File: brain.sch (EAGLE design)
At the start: 14 parts

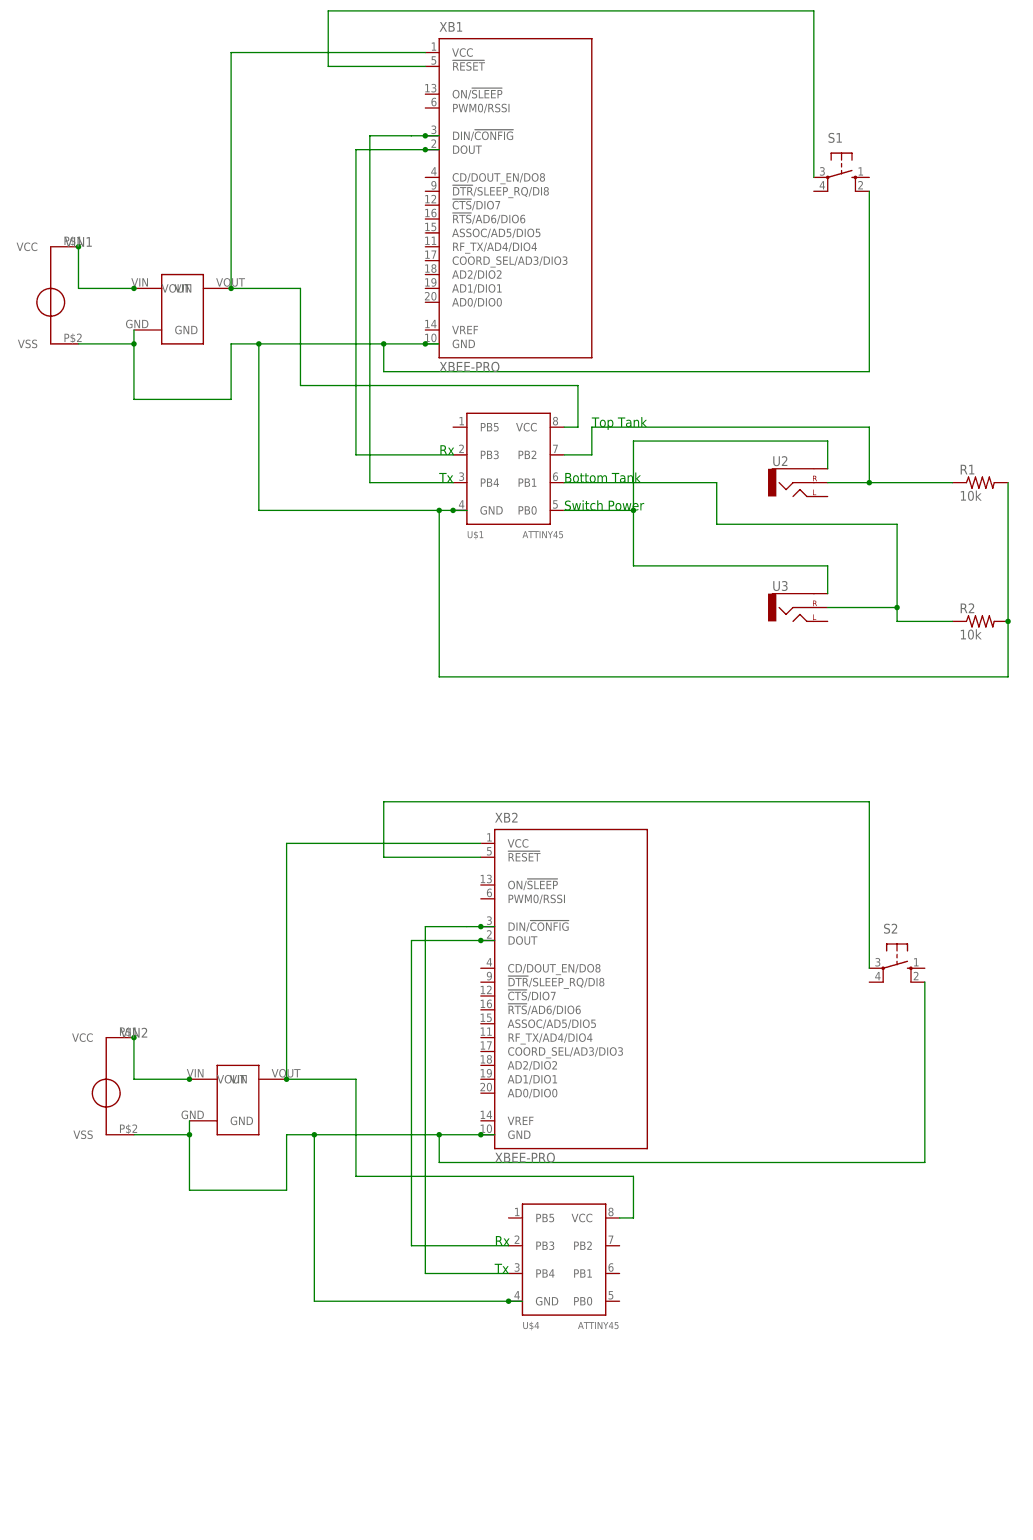
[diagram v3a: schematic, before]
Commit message: Switched the ATTINY45 to the proper package. Added error LED to receiving board. Bypass capacitors added to board. To consider: using vcc/gnd planes for capacitance as well.
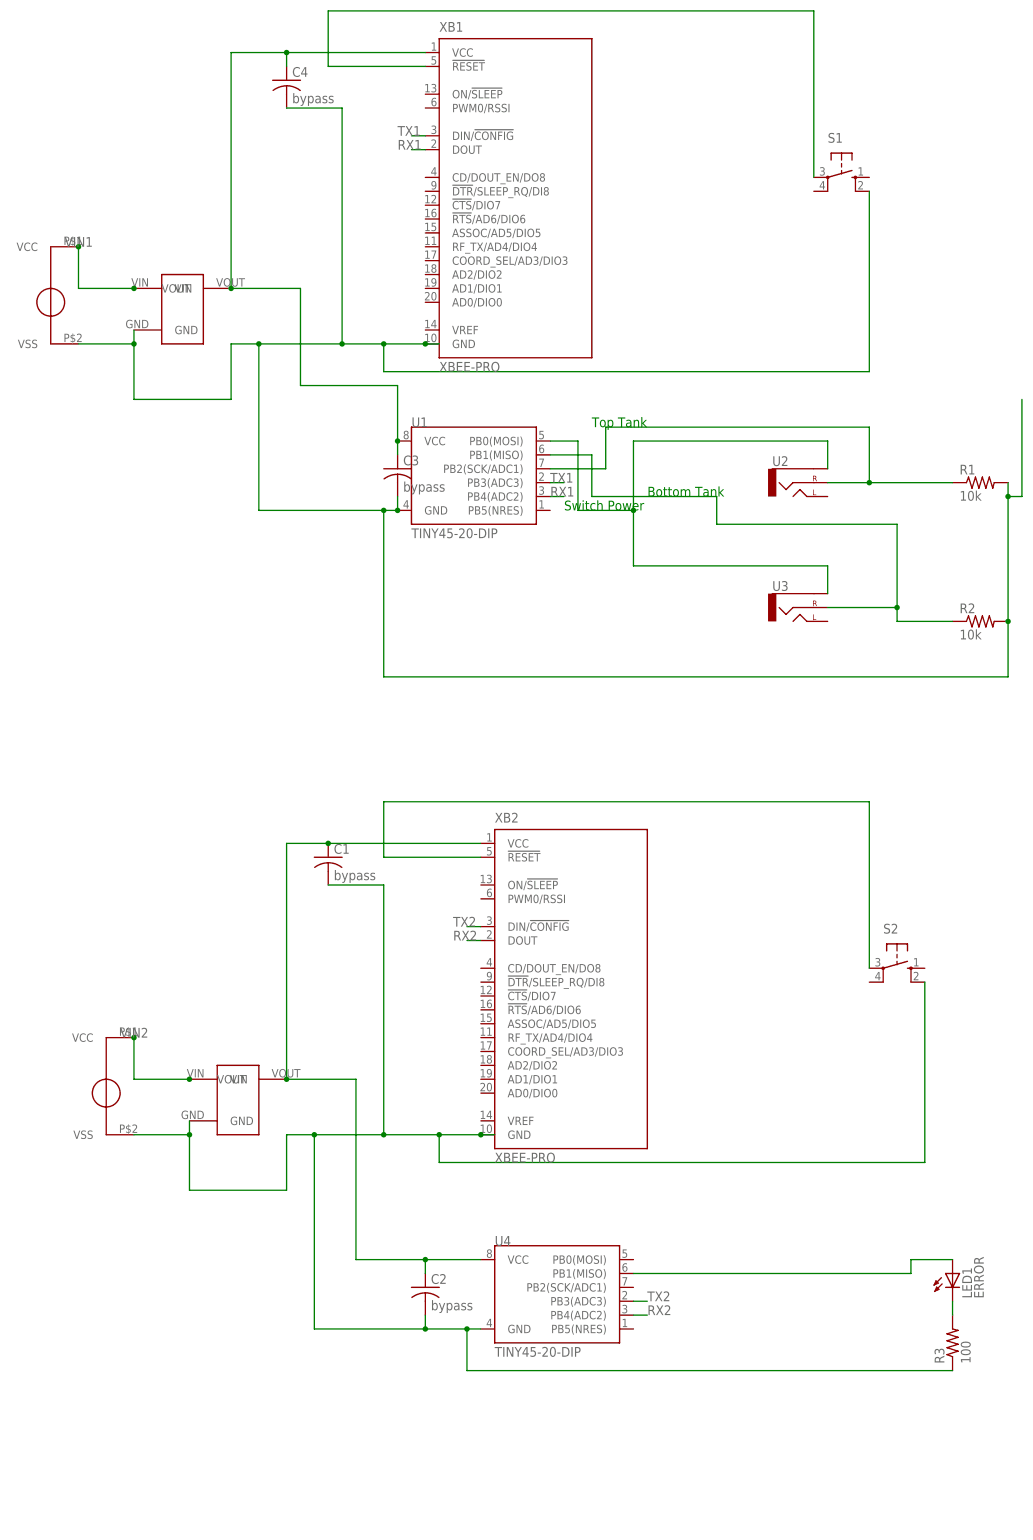
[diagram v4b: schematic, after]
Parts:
- removed U$1, U$4: ATTINY45, attiny45:ATTINY45
- added C1, C2, C3, C4: bypass, rcl:C-US050-025X075
- added LED1: ERROR, led:LED3MM
- added R3: 100, resistor:R-US_0207/10
- added U1, U4: TINY45-20-DIP, SparkFun-DigitalIC:ATTINY45TINY45-20-DIP
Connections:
- removed net N$11: U$1.PB4, XB1.DIN/!CONFIG
- removed net N$14: U$1.PB3, XB1.DOUT
- removed net N$7: U$4.PB4, XB2.DIN/!CONFIG
- removed net N$9: U$4.PB3, XB2.DOUT
- new net N$1: LED1.A, U4.PB1(MISO)
- new net N$5: LED1.C, R3.2
- new net RX1: U1.PB4(ADC2), XB1.DOUT
- new net RX2: U4.PB4(ADC2), XB2.DOUT
- new net TX1: U1.PB3(ADC3), XB1.DIN/!CONFIG
- new net TX2: U4.PB3(ADC3), XB2.DIN/!CONFIG
- net GND1: now also C3.2, C4.2, U1.GND; no longer U$1.GND
- net GND2: now also C1.2, C2.2, R3.1, U4.GND; no longer U$4.GND
- net N$2: now also U1.PB2(SCK/ADC1); no longer U$1.PB2
- net N$3: now also U1.PB1(MISO); no longer U$1.PB1
- net N$4: now also U1.PB0(MOSI); no longer U$1.PB0
- net VCC1: now also C3.1, C4.1, U1.VCC; no longer U$1.VCC
- net VOUT2: now also C1.1, C2.1, U4.VCC; no longer U$4.VCC
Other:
- note removed: "Rx"
- note removed: "Tx"

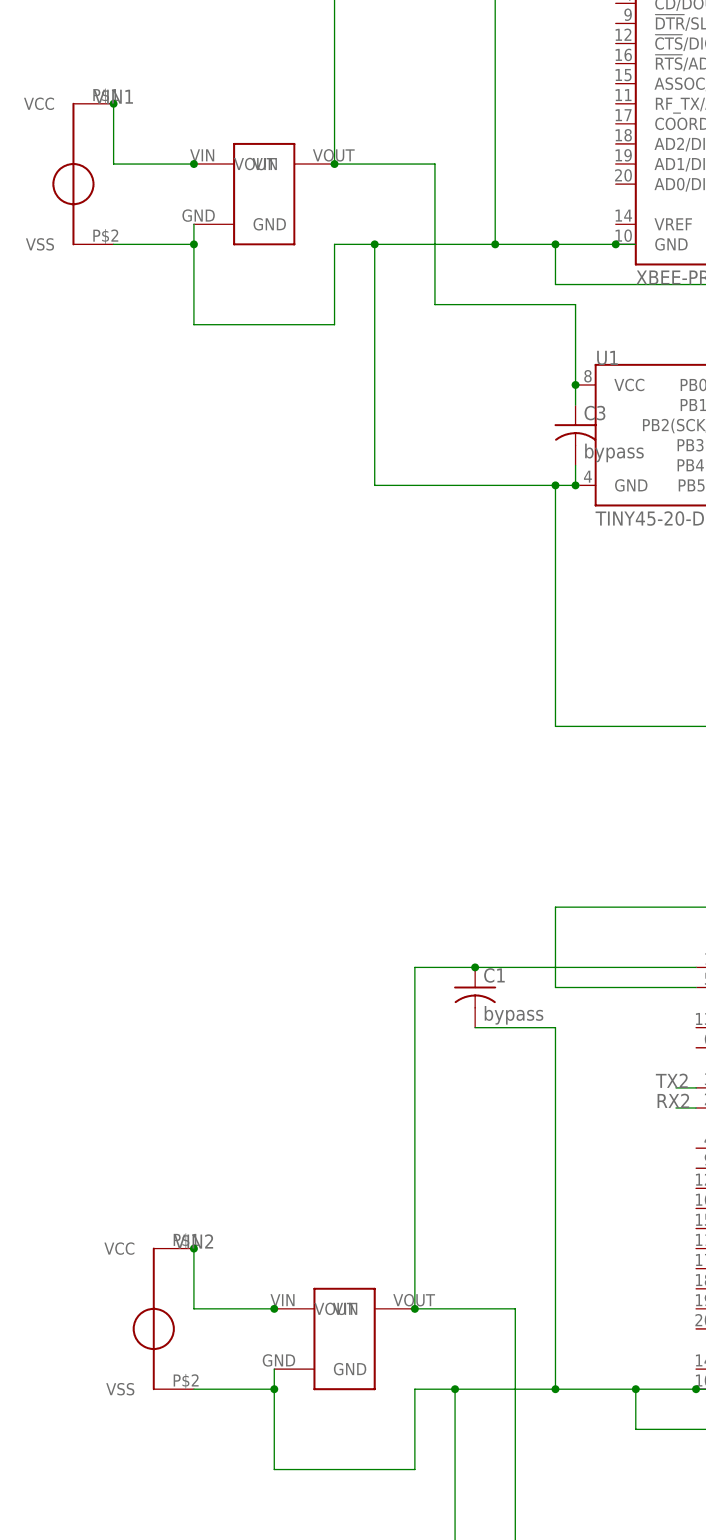
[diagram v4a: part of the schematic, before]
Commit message: Switched the LDO to the ST device.
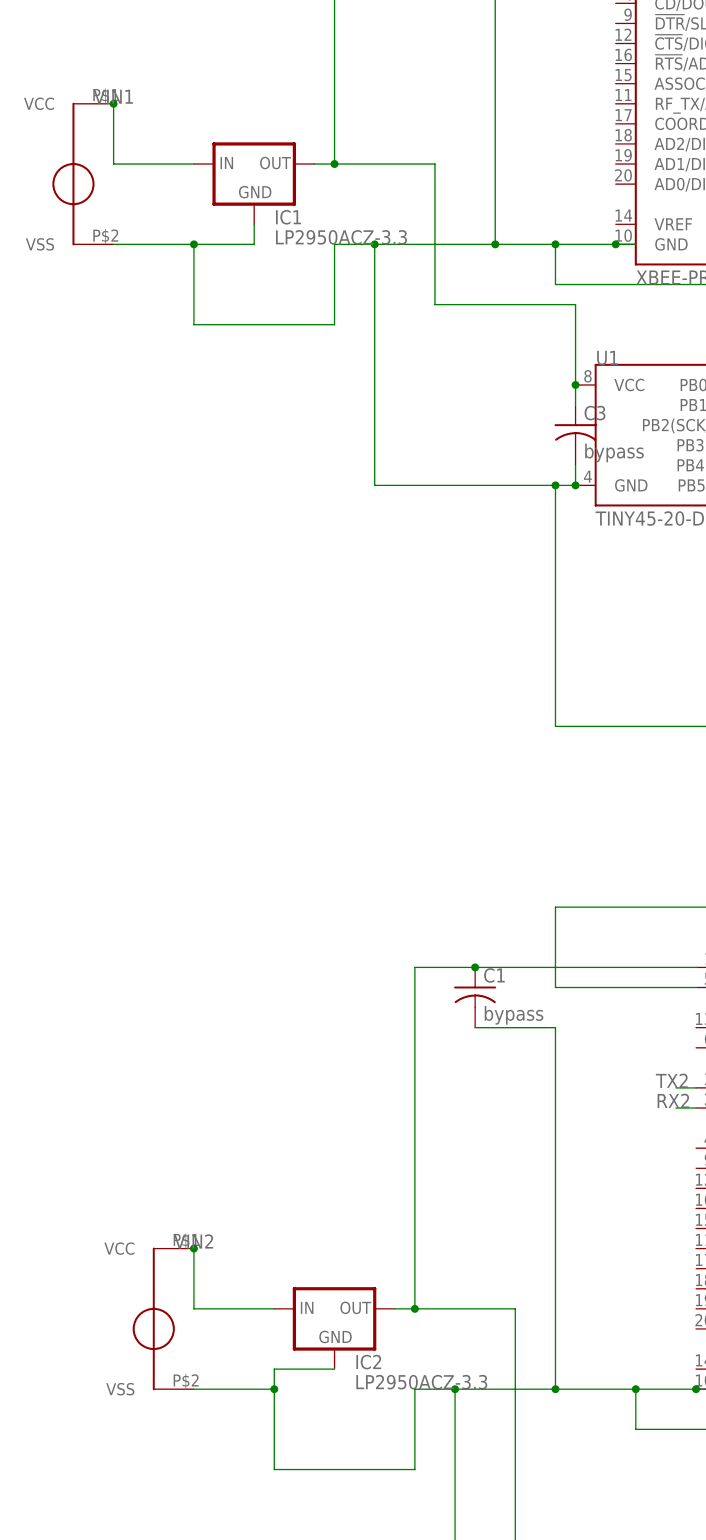
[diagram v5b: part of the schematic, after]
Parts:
- removed U$2, U$5: LP2950, seniordesign:LP2950
- added IC1, IC2: LP2950ACZ-3.3, v-reg:LP2950ACZ-3.3
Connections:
- net GND1: now also IC1.GND; no longer U$2.GND
- net GND2: now also IC2.GND; no longer U$5.GND
- net VCC1: now also IC1.OUT; no longer U$2.VOUT
- net VIN1: now also IC1.IN; no longer U$2.VIN
- net VIN2: now also IC2.IN; no longer U$5.VIN
- net VOUT2: now also IC2.OUT; no longer U$5.VOUT

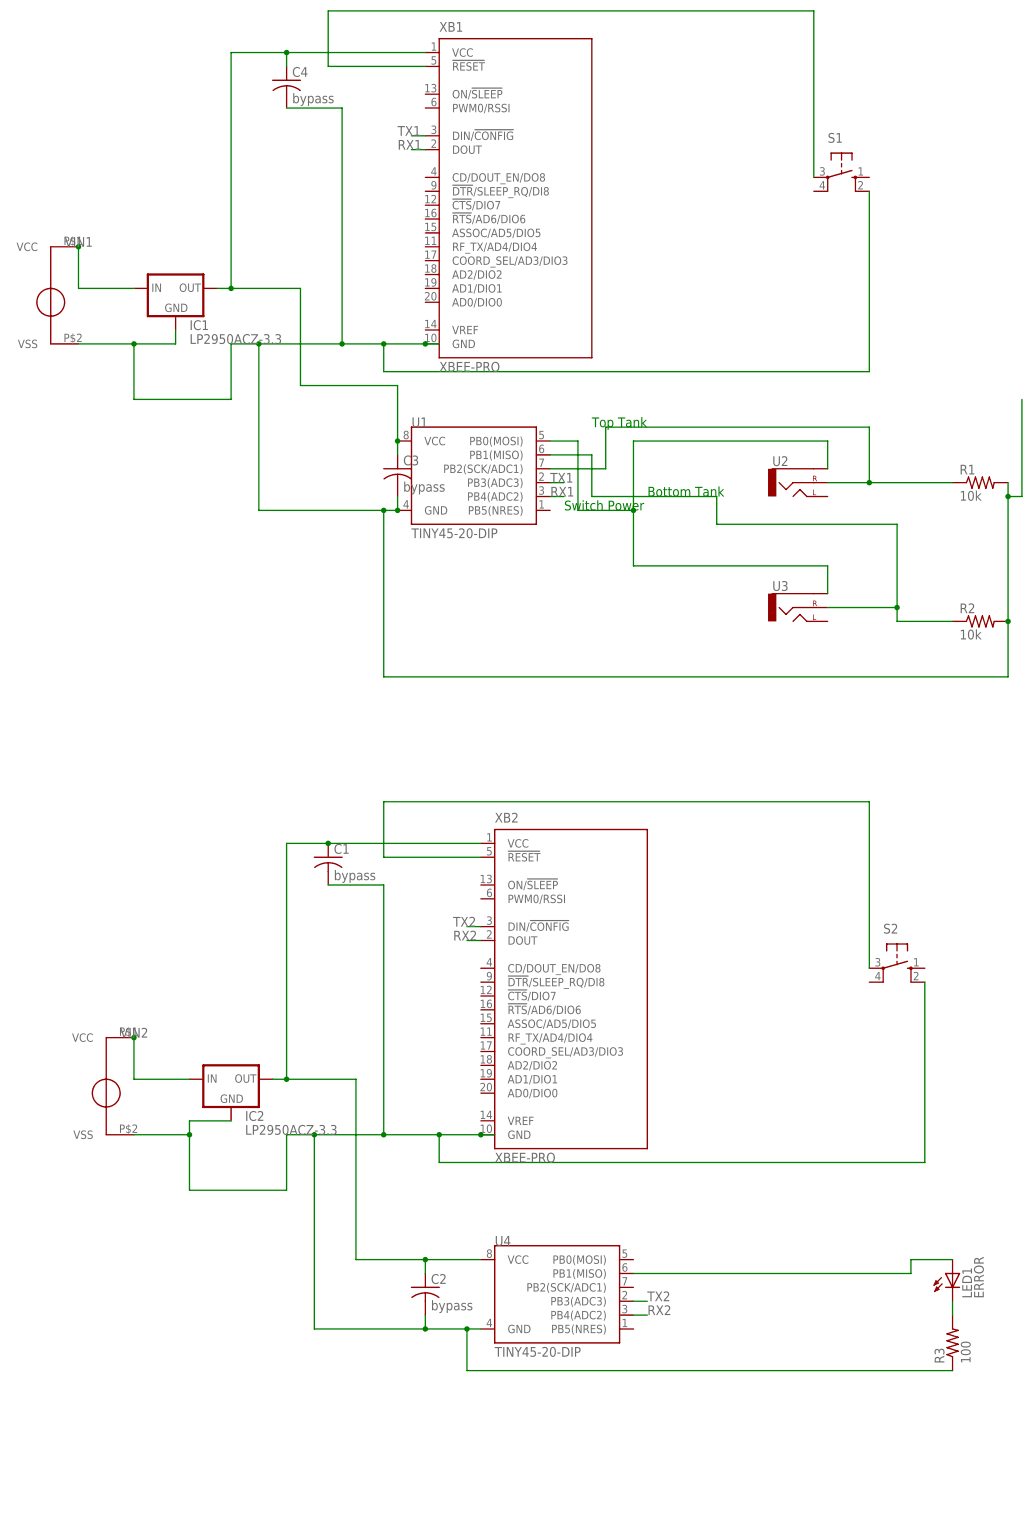
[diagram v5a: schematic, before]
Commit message: Added test terminals to board. Pre-routing.
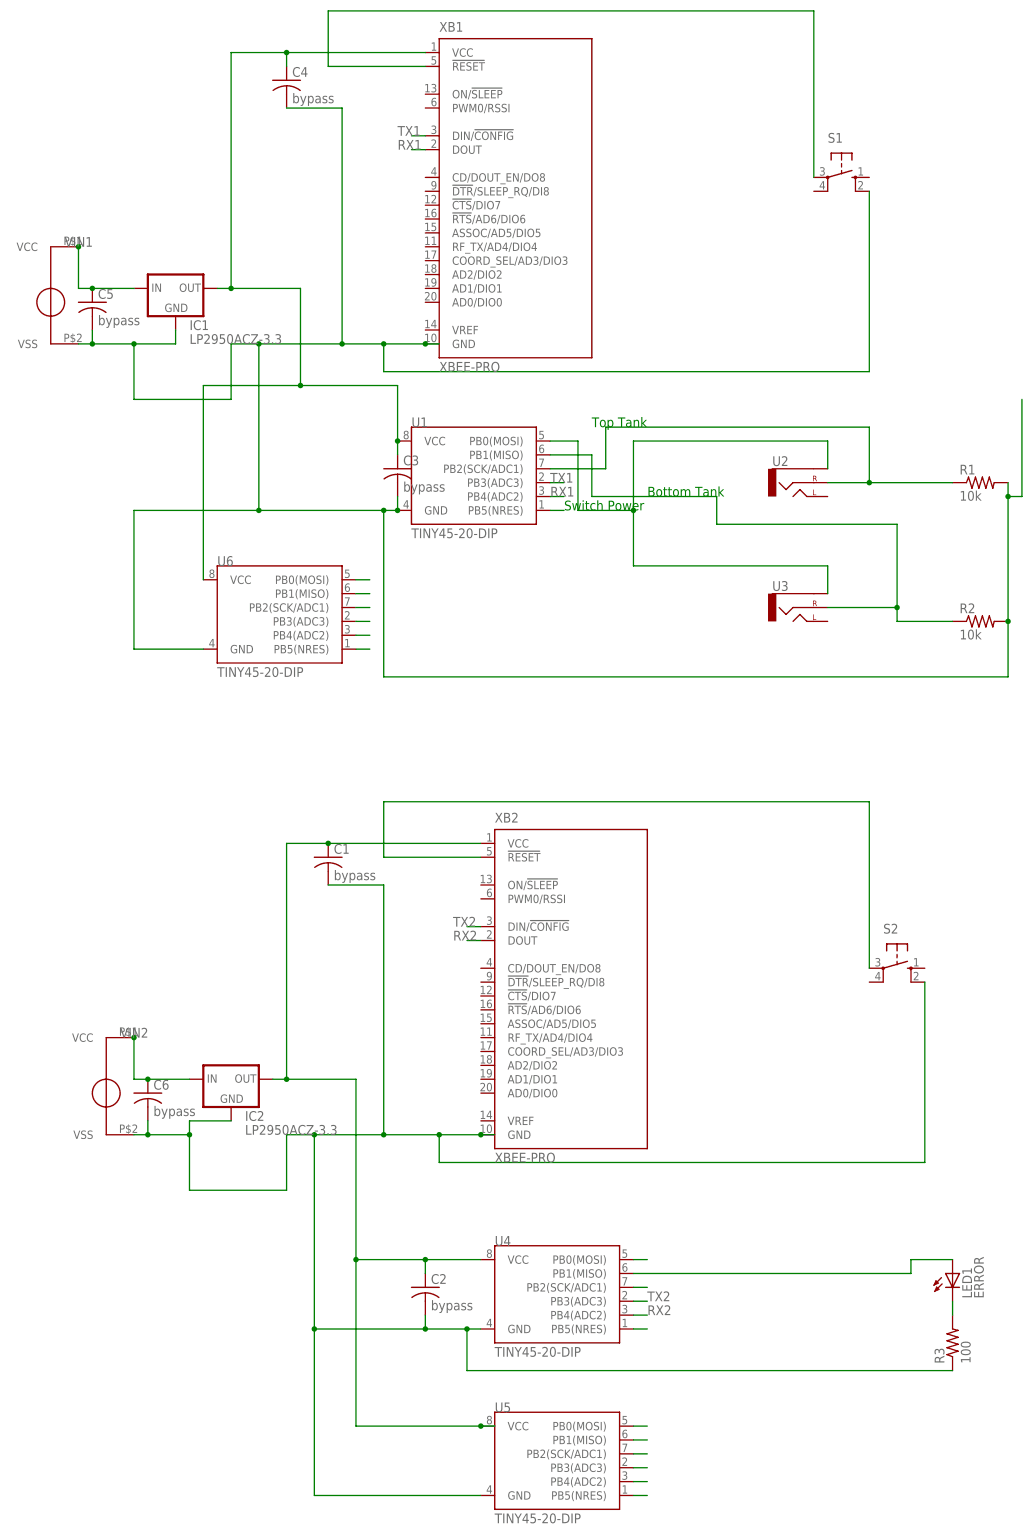
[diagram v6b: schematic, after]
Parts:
- added C5, C6: bypass, rcl:C-US050-025X075
- added U5, U6: TINY45-20-DIP, SparkFun-DigitalIC:ATTINY45TINY45-20-DIP
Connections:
- removed net N$1: LED1.A, U4.PB1(MISO)
- removed net N$2: R1.1, U1.PB2(SCK/ADC1), U2.RIGHT
- removed net N$3: R2.1, U1.PB1(MISO), U3.RIGHT
- removed net N$4: U1.PB0(MOSI), U2.SLEEVE, U3.SLEEVE
- new net N$14: U5.PB3(ADC3)
- new net N$7: U4.PB2(SCK/ADC1)
- new net PB01: U1.PB0(MOSI), U2.SLEEVE, U3.SLEEVE, U6.PB0(MOSI)
- new net PB02: U4.PB0(MOSI), U5.PB0(MOSI)
- new net PB11: R2.1, U1.PB1(MISO), U3.RIGHT, U6.PB1(MISO)
- new net PB12: LED1.A, U4.PB1(MISO), U5.PB1(MISO)
- new net PB21: R1.1, U1.PB2(SCK/ADC1), U2.RIGHT, U6.PB2(SCK/ADC1)
- new net PB51: U1.PB5(NRES), U6.PB5(NRES)
- new net PB52: U4.PB5(NRES), U5.PB5(NRES)
- net GND1: now also C5.2, U6.GND
- net GND2: now also C6.2, U5.GND
- net RX1: now also U6.PB4(ADC2)
- net RX2: now also U5.PB4(ADC2)
- net TX1: now also U6.PB3(ADC3)
- net TX2: now also U5.PB2(SCK/ADC1)
- net VCC1: now also U6.VCC
- net VIN1: now also C5.1
- net VIN2: now also C6.1
- net VOUT2: now also U5.VCC
